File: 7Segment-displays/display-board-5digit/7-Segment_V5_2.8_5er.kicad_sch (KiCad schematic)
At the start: 3 parts, among them J1 Conn_02x08_Odd_Even, U1 7Segment 3 digit CC_STH, U2 HDSM-443B_CC_2Digit_7Segment_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

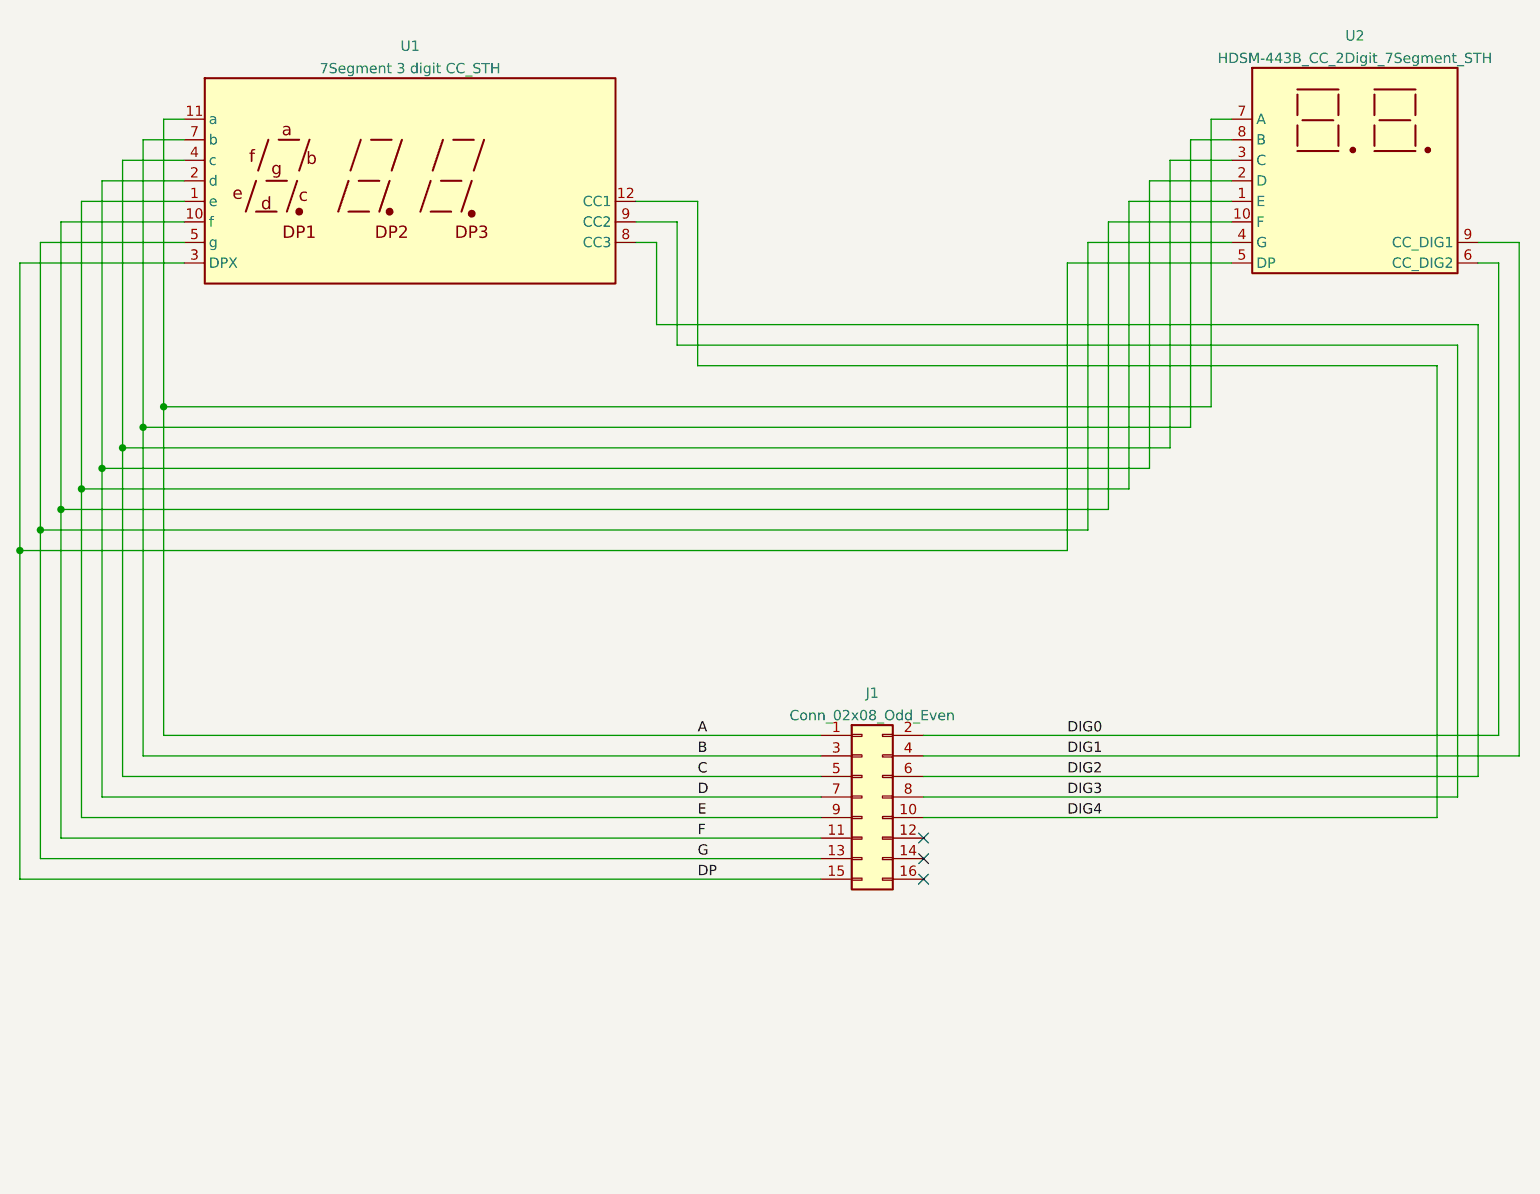
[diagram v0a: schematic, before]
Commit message: update 4/5/6 digit schematic and pcb to MF lib, add 3 digit to lib
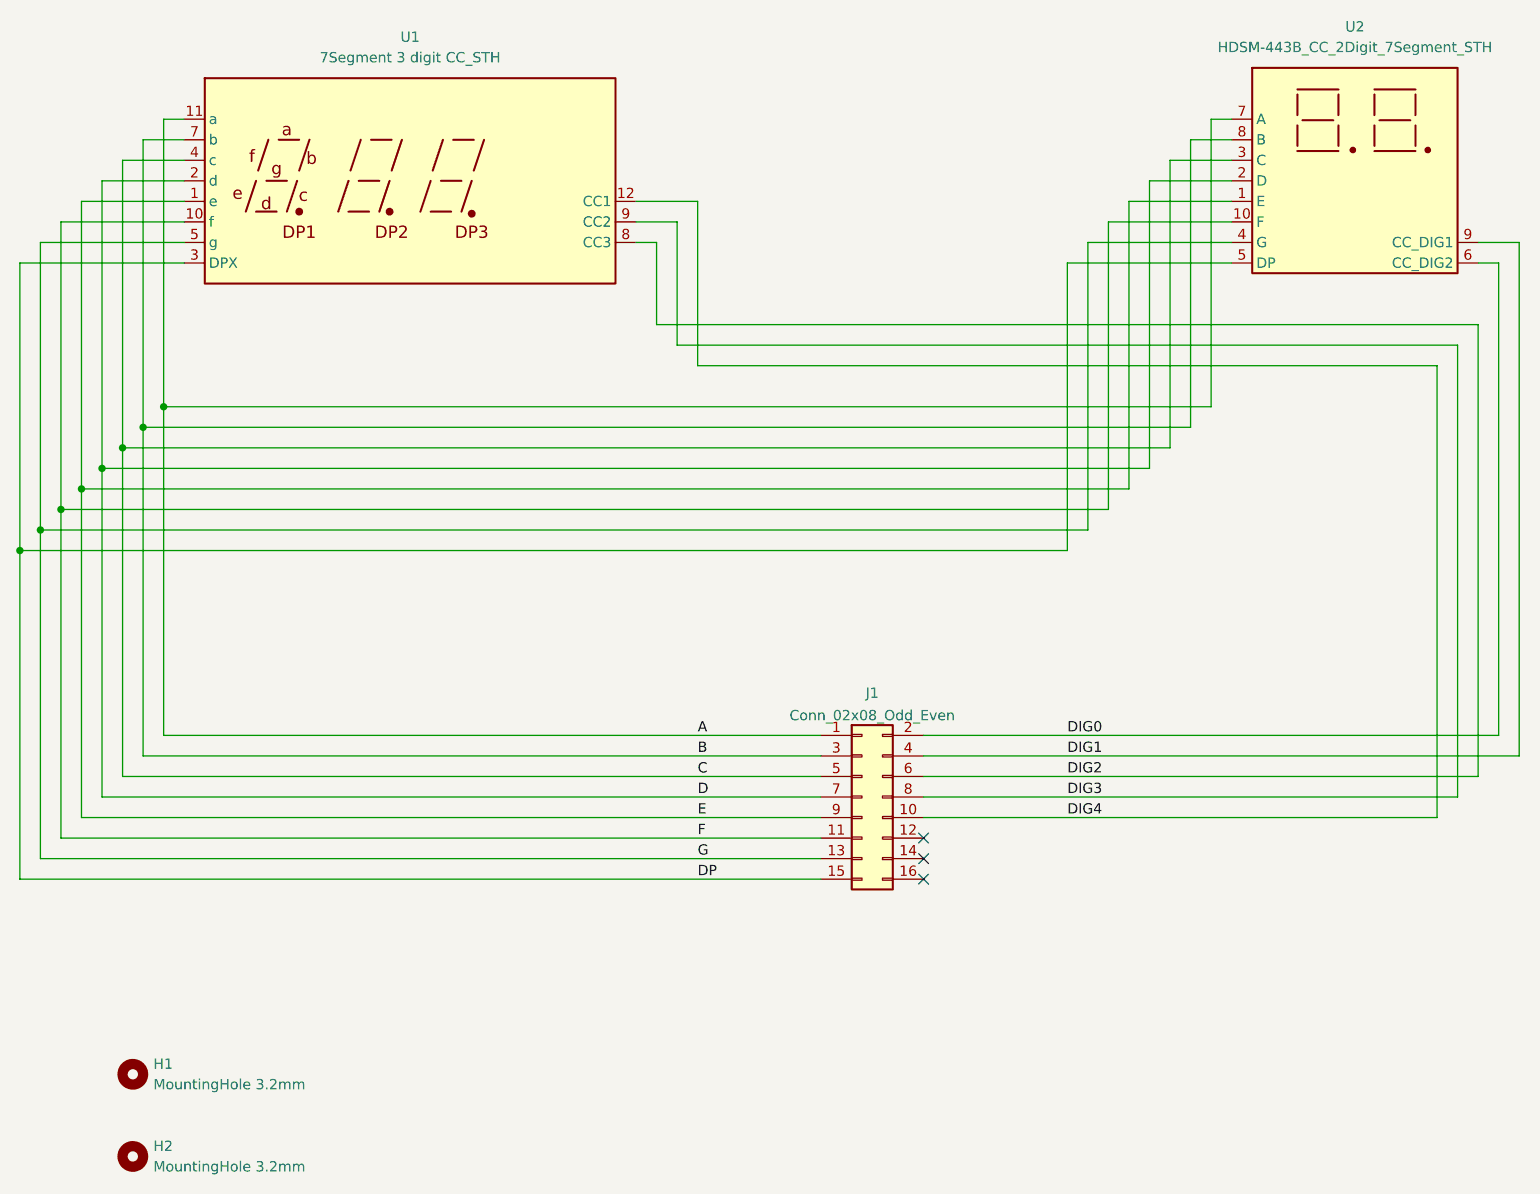
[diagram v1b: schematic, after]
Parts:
- added H1, H2: MountingHole 3.2mm, MountingHole:MountingHole_3.2mm_M3_Pad, symbol MobiFlight:MountingHole 3.2mm
- U1: footprint Display_7Segment:STH_7_3 Digits_0.28_CC -> MobiFlight:STH_7_3 Digits_0.28_CC; symbol Display_Character:7Segment 3 digit CC_STH -> MobiFlight:7Segment 3 digit common cathode STH
- U2: footprint Display_7Segment:STH_7_2 Digits_0.28_CC -> MobiFlight:STH_7_2 Digits_0.28_CC; symbol Display_Character:HDSM-443B_CC_2Digit_7Segment_STH -> MobiFlight:7Segment 2 digit common cathode STH
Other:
- company: (none) -> MobiFLight
- title: (none) -> 7 Segment Display Module, 5 digits
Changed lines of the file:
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@@
 	(generator_version "9.0")
 	(paper "A4")
+	(title_block
+		(title "7 Segment Display Module, 5 digits")
+		(date "2025-11")
+		(rev "V5.2")
+		(company "MobiFLight")
+	)
 	(junction
 		(at 38.1 68.58)
@@
 	)
 	(symbol
-		(lib_id "Display_Character:HDSM-443B_CC_2Digit_7Segment_STH")
+		(lib_id "MobiFlight:MountingHole 3.2mm")
+		(at 41.91 153.67 0)
+		(unit 1)
+		(exclude_from_sim yes)
+		(in_bom no)
+		(on_board yes)
+		(dnp no)
+		(fields_autoplaced yes)
+		(property "Reference" "H2"
+			(at 44.45 152.3999 0)
+			(effects
+				(font
+					(size 1.27 1.27)
+				)
+				(justify left)
+			)
+		)
+		(property "Value" "MountingHole 3.2mm"
+			(at 44.45 154.9399 0)
+			(effects
+				(font
+					(size 1.27 1.27)
+				)
+				(justify left)
+			)
+		)
+		(property "Footprint" "MountingHole:MountingHole_3.2mm_M3_Pad"
+			(at 41.91 153.67 0)
+			(effects
+				(font
+					(size 1.27 1.27)
+				)
+				(hide yes)
+			)
+		)
+		(property "Datasheet" "~"
+			(at 41.91 153.67 0)
+			(effects
+				(font
+					(size 1.27 1.27)
+				)
+				(hide yes)
+			)
+		)
+		(property "Description" "Mounting Hole without connection"
+			(at 41.91 153.67 0)
+			(effects
+				(font
+					(size 1.27 1.27)
+				)
+				(hide yes)
+			)
+		)
+		(instances
+			(project ""
+				(path "/5a88ad9f-c8ab-49a3-b9f4-b339518a12ac"
+					(reference "H2")
+					(unit 1)
+				)
+			)
+		)
+	)
+	(symbol
+		(lib_id "MobiFlight:MountingHole 3.2mm")
+		(at 41.91 143.51 0)
+		(unit 1)
+		(exclude_from_sim yes)
+		(in_bom no)
+		(on_board yes)
+		(dnp no)
+		(fields_autoplaced yes)
+		(property "Reference" "H1"
+			(at 44.45 142.2399 0)
+			(effects
+				(font
+					(size 1.27 1.27)
+				)
+				(justify left)
+			)
+		)
+		(property "Value" "MountingHole 3.2mm"
+			(at 44.45 144.7799 0)
+			(effects
+				(font
+					(size 1.27 1.27)
+				)
+				(justify left)
+			)
+		)
+		(property "Footprint" "MountingHole:MountingHole_3.2mm_M3_Pad"
+			(at 41.91 143.51 0)
+			(effects
+				(font
+					(size 1.27 1.27)
+				)
+				(hide yes)
+			)
+		)
+		(property "Datasheet" "~"
+			(at 41.91 143.51 0)
+			(effects
+				(font
+					(size 1.27 1.27)
+				)
+				(hide yes)
+			)
+		)
+		(property "Description" "Mounting Hole without connection"
+			(at 41.91 143.51 0)
+			(effects
+				(font
+					(size 1.27 1.27)
+				)
+				(hide yes)
+			)
+		)
+		(instances
+			(project ""
+				(path "/5a88ad9f-c8ab-49a3-b9f4-b339518a12ac"
+					(reference "H1")
+					(unit 1)
+				)
+			)
+		)
+	)
+	(symbol
+		(lib_id "MobiFlight:7Segment 2 digit common cathode STH")
 		(at 193.04 33.02 0)
 		(unit 1)
@@
 		(fields_autoplaced yes)
 		(property "Reference" "U2"
-			(at 193.04 15.0835 0)
+			(at 193.04 13.97 0)
 			(effects
 				(font
@@
 		)
 		(property "Value" "HDSM-443B_CC_2Digit_7Segment_STH"
-			(at 193.04 17.8586 0)
-			(effects
-				(font
-					(size 1.27 1.27)
-				)
-			)
-		)
-		(property "Footprint" "Display_7Segment:STH_7_2 Digits_0.28_CC"
+			(at 193.04 16.51 0)
+			(effects
+				(font
+					(size 1.27 1.27)
+				)
+			)
+		)
+		(property "Footprint" "MobiFlight:STH_7_2 Digits_0.28_CC"
 			(at 193.04 48.26 0)
 			(effects
@@
 	)
 	(symbol
-		(lib_id "Display_Character:7Segment 3 digit CC_STH")
+		(lib_id "MobiFlight:7Segment 3 digit common cathode STH")
 		(at 76.2 33.02 0)
 		(unit 1)
@@
 		(fields_autoplaced yes)
 		(property "Reference" "U1"
-			(at 76.2 16.3535 0)
+			(at 76.2 15.24 0)
 			(effects
 				(font
@@
 		)
 		(property "Value" "7Segment 3 digit CC_STH"
-			(at 76.2 19.1286 0)
-			(effects
-				(font
-					(size 1.27 1.27)
-				)
-			)
-		)
-		(property "Footprint" "Display_7Segment:STH_7_3 Digits_0.28_CC"
+			(at 76.2 17.78 0)
+			(effects
+				(font
+					(size 1.27 1.27)
+				)
+			)
+		)
+		(property "Footprint" "MobiFlight:STH_7_3 Digits_0.28_CC"
 			(at 76.2 48.26 0)
 			(effects
